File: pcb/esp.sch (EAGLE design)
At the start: 28 parts, among them Q1 2N3904, Q2 2N3904

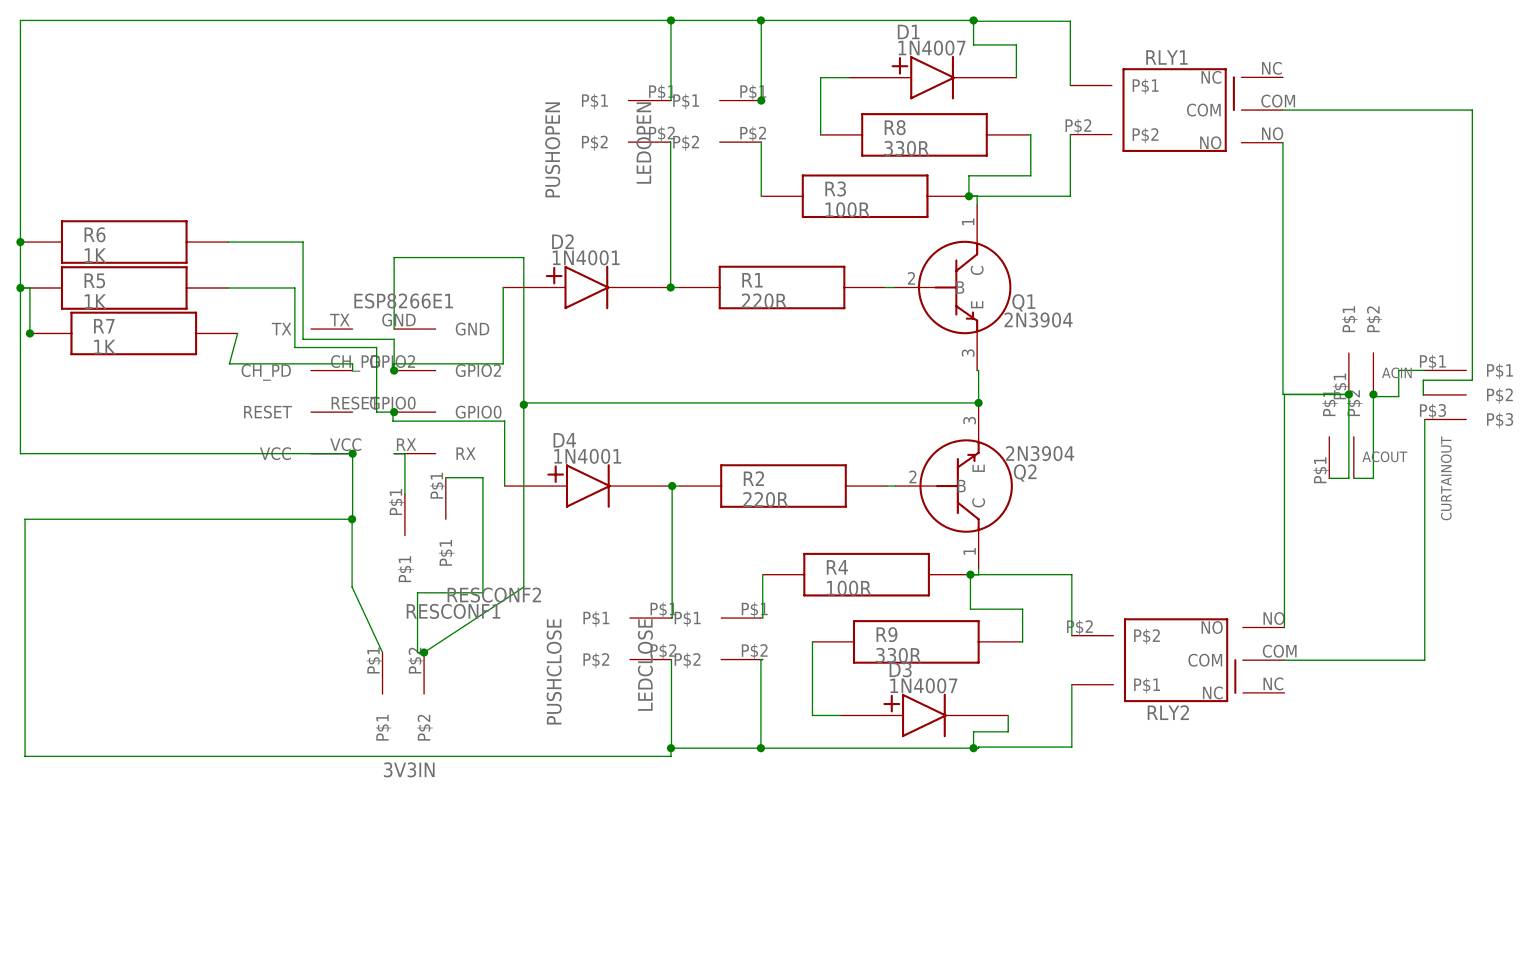
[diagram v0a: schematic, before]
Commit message: Remove ignored EAGLE files. Separate the README files. Renew circuit schematic and board images.
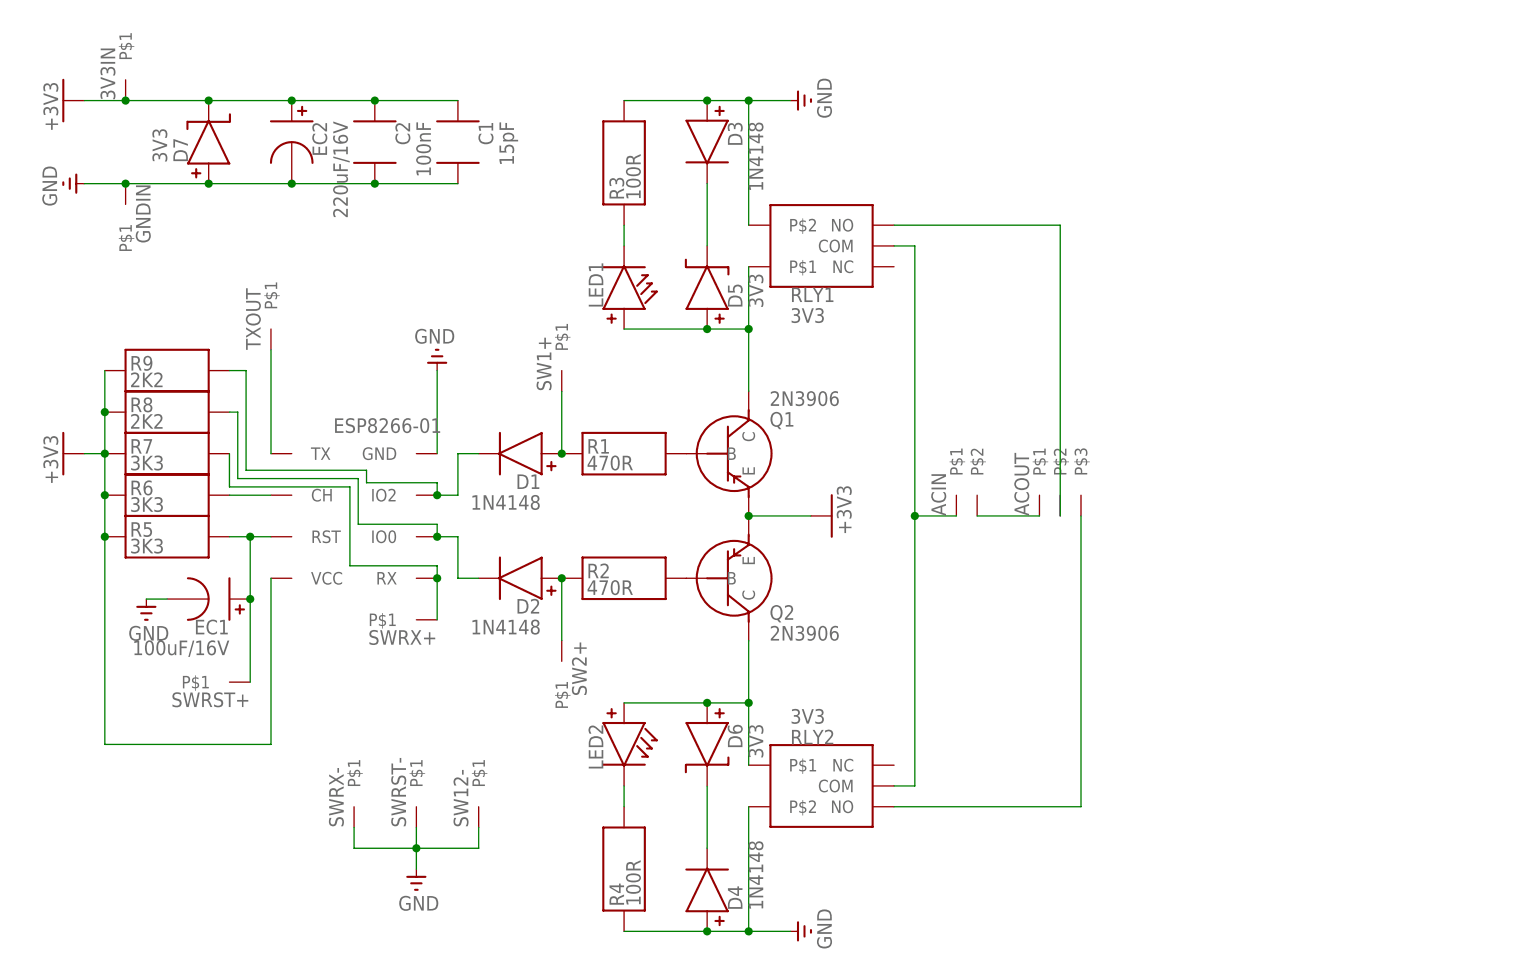
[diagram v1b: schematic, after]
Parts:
- removed CURTAINOUT: CON3CON5.0S3T, simple-parts:CON3CON5.0S3T
- removed ESP8266E1: ESP8266E01ESP8266E01, simple-parts:ESP8266E01ESP8266E01
- removed LEDCLOSE, LEDOPEN, PUSHCLOSE, PUSHOPEN: PINPLUG2PINPLUG2, simple-parts:PINPLUG2PINPLUG2
- removed RESCONF1, RESCONF2: PINPLUG1PINPLUG1, simple-parts:PINPLUG1PINPLUG1
- added C1: 15pF, simple-parts:CAPACITORCERCAP3.2S
- added C2: 100nF, simple-parts:CAPACITORCERCAP5.6S
- added D5, D6, D7: 3V3, simple-parts:ZENDIODEZD6.0S2.0D
- added EC1: 100uF/16V, simple-parts:ECAPACITORECAP3.2S5.0D
- added EC2: 220uF/16V, simple-parts:ECAPACITORECAP3.2S5.0D
- added ESP8266-01: ESP8266E01ESP8266E01, simple-parts:ESP8266E01ESP8266E01
- added GNDIN, SW1+, SW12-, SW2+, SWRST+, SWRST-, SWRX+, SWRX-, TXOUT: (no value), simple-parts:CON1PINPLUG1
- added LED1, LED2: (no value), simple-parts:LEDLED3.2S5.0D
- 3V3IN: value PINPLUG2PINPLUG2 -> (none); device simple-parts:PINPLUG2PINPLUG2 -> simple-parts:CON1PINPLUG1
- ACOUT: value CON2CON5.0S2T -> CON3CON5.0S3T; device simple-parts:CON2CON5.0S2T -> simple-parts:CON3CON5.0S3T
- D1, D3: value 1N4007 -> 1N4148; device simple-parts:RECTDIODERD8.0S2.6D -> simple-parts:RECTDIODERD5.0S1.8D
- D2, D4: value 1N4001 -> 1N4148; device simple-parts:RECTDIODERD8.0S2.6D -> simple-parts:RECTDIODERD5.0S1.8D
- Q1, Q2: value 2N3904 -> 2N3906; device simple-parts:BJTNPNTO92NPN -> simple-parts:BJTPNPTO92
- R1, R2: value 220R -> 470R
- R5, R6, R7: value 1K -> 3K3
- R8, R9: value 330R -> 2K2
- RLY1, RLY2: value (none) -> 3V3; device simple-parts:RELAY5RLY12W12L -> simple-parts:RELAY5RLY15W19L
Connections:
- removed net N$17 (its old number): D3.P+, R9.P$1
- removed net N$19: LEDCLOSE.P$1, R4.P$1
- removed net N$21: D1.P+, R8.P$1
- new net +3V3: 3V3IN.P$1, C1.P$1, C2.P$1, D7.P-, EC2.P+, ESP8266-01.VCC, Q1.E, Q2.E, R5.P$1, R6.P$1, R7.P$1, R8.P$1, R9.P$1
- new net GND: C1.P$2, C2.P$2, D3.P+, D4.P+, D7.P+, EC1.P-, EC2.P-, ESP8266-01.GND, GNDIN.P$1, R3.P$2, R4.P$1, RLY1.P$2, RLY2.P$2, SW12-.P$1, SWRST-.P$1, SWRX-.P$1
- new net N$18: D2.P+, R2.P$1, SW2+.P$1
- new net N$2: ESP8266-01.CH, R6.P$2
- new net N$23: D1.P-, ESP8266-01.IO2, R9.P$2
- net N$1: now also LED2.P-, R4.P$2; no longer Q1.C, R3.P$2, R8.P$2, RLY1.P$2
- net N$10: now also EC1.P+, ESP8266-01.RST, R5.P$2, SWRST+.P$1; no longer 3V3IN.P$1, D1.P-, D3.P-, ESP8266E1.VCC, LEDCLOSE.P$2, LEDOPEN.P$1, PUSHCLOSE.P$2, PUSHOPEN.P$1, R5.P$1, R6.P$1, R7.P$1, RLY1.P$1, RLY2.P$1
- net N$11: now also ACOUT.P$3, RLY2.NO; no longer D4.P-, PUSHCLOSE.P$1, R2.P$1
- net N$12: now also D5.P+, LED1.P+, Q1.C, RLY1.P$1; no longer D2.P+, ESP8266E1.GPIO2, R6.P$2
- net N$13: now also ESP8266-01.TX, TXOUT.P$1; no longer D4.P+, ESP8266E1.GPIO0, R5.P$2
- net N$14: now also D3.P-, D5.P-; no longer 3V3IN.P$2, ESP8266E1.GND, Q1.E, Q2.E, RESCONF2.P$1
- net N$15: now also ACOUT.P$2, RLY1.NO; no longer CURTAINOUT.P$3, RLY2.COM
- net N$16: now also ACIN.P$2, ACOUT.P$1; no longer CURTAINOUT.P$2, RLY1.COM
- net N$20: now also ACIN.P$1, RLY1.COM, RLY2.COM; no longer ESP8266E1.CH_PD, R7.P$2
- net N$3: now also ESP8266-01.RX, R7.P$2, SWRX+.P$1; no longer D2.P-, PUSHOPEN.P$2, R1.P$1
- net N$5: now also D1.P+, R1.P$1, SW1+.P$1; no longer LEDOPEN.P$2, R3.P$1
- net N$6: now also D2.P-, ESP8266-01.IO0, R8.P$2; no longer ACIN.P$2, ACOUT.P$2, CURTAINOUT.P$1
- net N$7: now also D6.P+, LED2.P+, RLY2.P$1; no longer R4.P$2, R9.P$2, RLY2.P$2
- net N$8: now also LED1.P-, R3.P$1; no longer ESP8266E1.RX, RESCONF1.P$1
- net N$9: now also D4.P-, D6.P-; no longer ACIN.P$1, ACOUT.P$1, RLY1.NO, RLY2.NO
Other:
- moved on the sheet: D1, D2, D3, D4
